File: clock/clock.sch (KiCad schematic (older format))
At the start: 166 parts, among them J1 Conn_02x05_Odd_Even, P1 Conn_WallPlug, T1 120 to 12, U1 74HC596, U10 74HC596, U11 LPC804-TSSOP24, U2 74HC596, U3 74HC596, U4 74HC596, U5 74HC596, U6 74HC596, U7 L78L33ABU, U8 74HC596, U9 74HC596

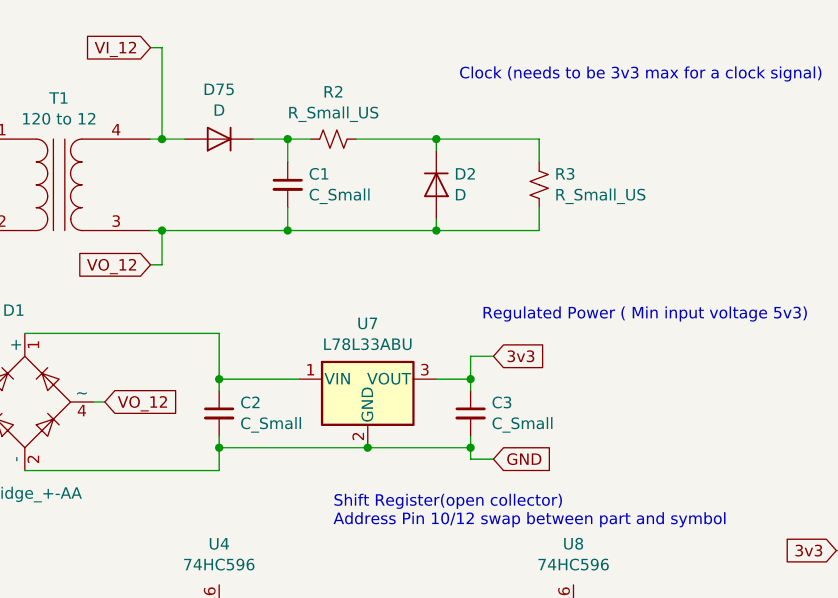
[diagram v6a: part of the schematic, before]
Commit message: Working on placing all 72 castellated holes for the LEDs.
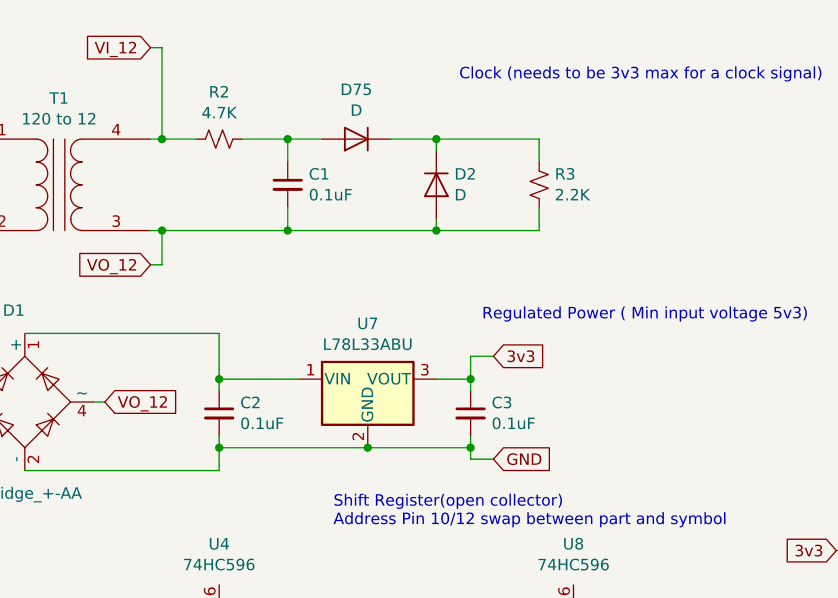
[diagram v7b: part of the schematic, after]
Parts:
- C1, C2, C3: value C_Small -> 0.1uF; footprint (none) -> Capacitor_SMD:C_0805_2012Metric
- D1: footprint (none) -> Diode_SMD:Diode_Bridge_Diotec_ABS
- D10, D11, D12, D13, D14, D15, D16, D17, D18, D19, D20, D21, D22, D23, D24, D25, D26, D27, D28, D29, D3, D30, D31, D32, D33, D34, D35, D36, D37, D38, D39, D4, D40, D41, D42, D43, D44, D45, D46, D47, D48, D49, D5, D50, D51, D52, D53, D54, D55, D56, D57, D58, D59, D6, D60, D61, D62, D63, D64, D65, D66, D67, D68, D69, D7, D70, D71, D72, D73, D74, D8, D9: footprint (none) -> LTST-S110KGKT_castellated:LTST-S110KGKT_castellated
- D2, D75: footprint (none) -> Diode_SMD:D_0805_2012Metric
- J1: footprint (none) -> Connector_PinHeader_1.27mm:PinHeader_2x05_P1.27mm_Vertical
- R10, R11, R12, R13, R14, R15, R16, R17, R18, R19, R20, R21, R22, R23, R24, R25, R26, R27, R28, R29, R30, R31, R32, R33, R34, R35, R36, R37, R38, R39, R4, R40, R41, R42, R43, R44, R45, R46, R47, R48, R49, R5, R50, R51, R52, R53, R54, R55, R56, R57, R58, R59, R6, R60, R61, R62, R63, R64, R65, R66, R67, R68, R69, R7, R70, R71, R72, R73, R74, R75, R8, R9: footprint (none) -> Resistor_SMD:R_0805_2012Metric
- R2: value R_Small_US -> 4.7K
- R3: value R_Small_US -> 2.2K
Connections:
- net VI_12: now also R2.2; no longer D75.2 (A)
- net at D2.1 (K), R3.2: now also D75.1 (K); no longer R2.1
- new net: C1.1, D75.2 (A), R2.1
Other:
- moved on the sheet: D75, R2

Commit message: Working on moving the castellated holes to the new outline. Saving progress.
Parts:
- D10, D11, D12, D13, D14, D15, D16, D17, D18, D19, D20, D21, D22, D23, D24, D25, D26, D27, D28, D29, D3, D30, D31, D32, D33, D34, D35, D36, D37, D38, D39, D4, D40, D41, D42, D43, D44, D45, D46, D47, D48, D49, D5, D50, D51, D52, D53, D54, D55, D56, D57, D58, D59, D6, D60, D61, D62, D63, D64, D65, D66, D67, D68, D69, D7, D70, D71, D72, D73, D74, D8, D9: footprint LTST-S110KGKT_castellated:LTST-S110KGKT_castellated -> LTST-S110KGKT_castellated:LTST-S110KGKT_castellated_silkV1
- P1: footprint (none) -> Connector_Phoenix_GMSTB:PhoenixContact_GMSTBA_2,5_2-G-7,62_1x02_P7.62mm_Horizontal
- R2, R3: footprint (none) -> Resistor_THT:R_Axial_DIN0204_L3.6mm_D1.6mm_P7.62mm_Horizontal
- U1, U10, U2, U3, U4, U5, U6, U8, U9: footprint (none) -> Package_SO:SOP-16_4.4x10.4mm_P1.27mm
- U11: footprint (none) -> Package_SO:TSSOP-24_4.4x7.8mm_P0.65mm
